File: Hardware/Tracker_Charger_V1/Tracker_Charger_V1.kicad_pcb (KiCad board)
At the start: 4 copper layers, 100 x 100 mm, 51 parts, among them J1 USB_C_USB20, J2 GSB3CN1130DSHR, J3 GSB3CN1130DSHR, J4 GSB3CN1130DSHR, J6 GSB3CN1130DSHR, J7 GSB3CN1130DSHR, SW1 SW_Push, SW2 SW_Push, SW3 SW_Push, SW4 SW_Push, SW5 SW_Push, SW6 SW_Push, U1 ESP32-C3-MINI-1-N4, U2 IN-PI15TAT5R5G5B, U3 RT8010, U6 IN-PI15TAT5R5G5B, U7 IN-PI15TAT5R5G5B, U8 IN-PI15TAT5R5G5B, U9 IN-PI15TAT5R5G5B

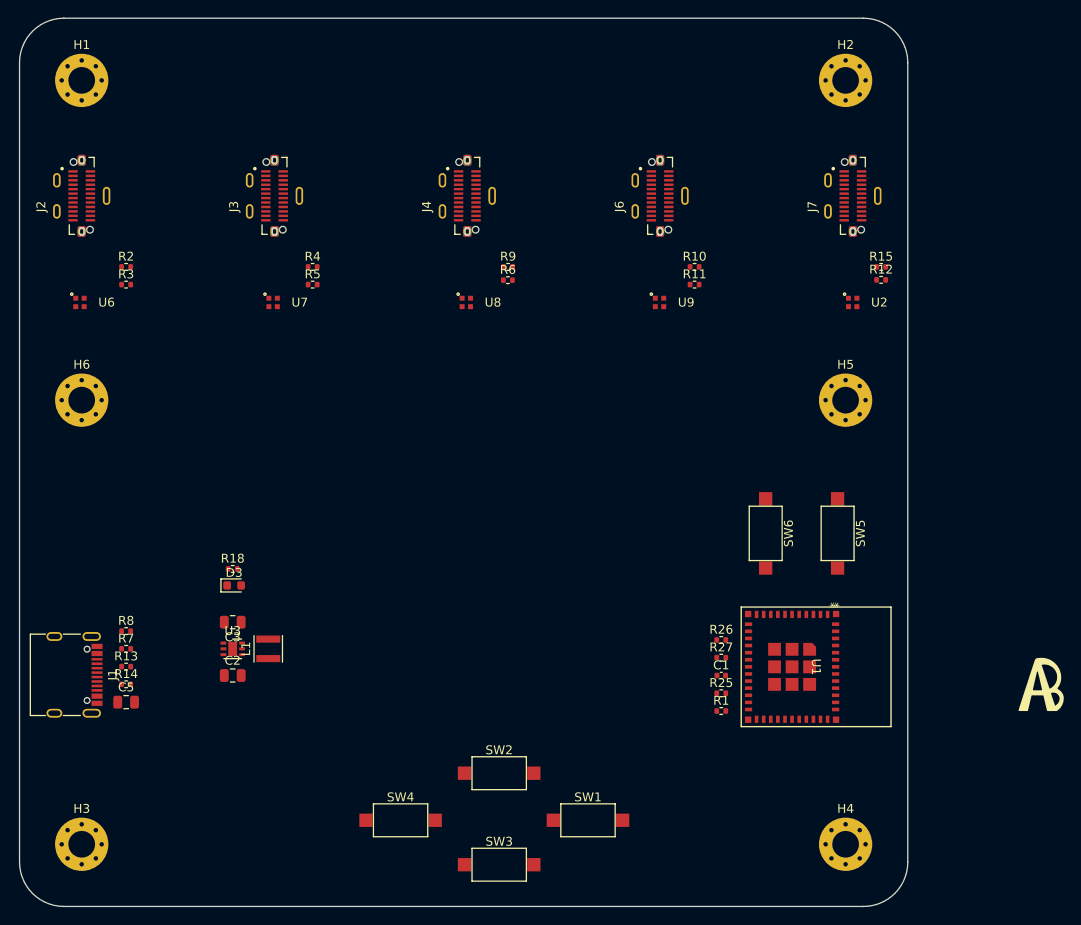
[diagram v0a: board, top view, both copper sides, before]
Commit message: Updated/Added Footprints
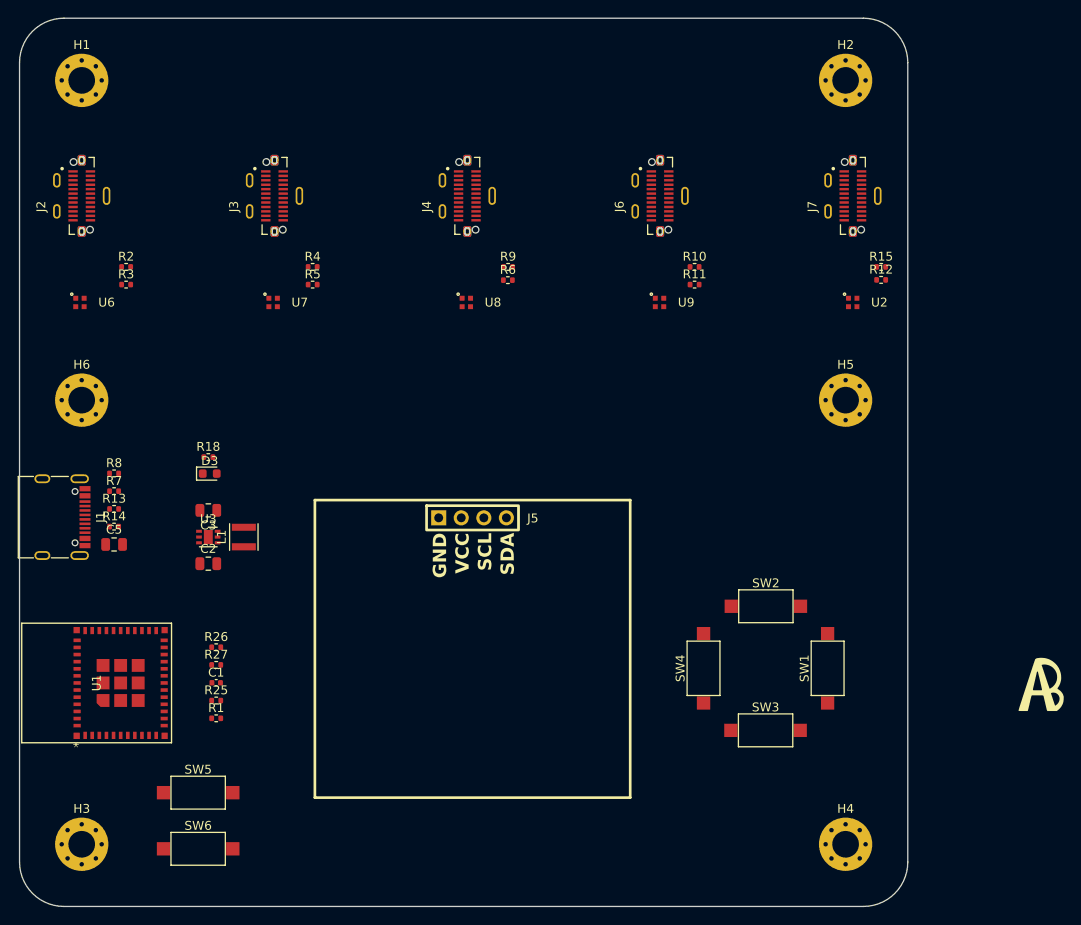
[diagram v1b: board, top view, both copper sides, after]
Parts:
- added J5: SSD1306_I2C_128x64, 00_tracker_fp:SSD1306_12864_I2C_13in, F.Cu at (141.0, 106.2)
- moved U1 81.0 mm to (98.7, 124.8), turned to 90 degrees
- moved SW5 77.7 mm to (110.1, 137.2), turned to 0 degrees
- moved SW6 73.1 mm to (110.1, 143.5), turned to 0 degrees
- moved C1 56.9 mm to (112.1, 124.8)
- moved R1 56.9 mm to (112.1, 128.8)
- moved R25 56.9 mm to (112.1, 126.8)
- moved R26 56.9 mm to (112.1, 120.8)
- moved R27 56.9 mm to (112.1, 122.8)
- moved SW4 38.2 mm to (167.0, 123.2), turned to 90 degrees
- moved SW2 35.4 mm to (174.0, 116.2)
- moved SW3 33.6 mm to (174.0, 130.2)
- moved SW1 31.9 mm to (181.0, 123.2), turned to 90 degrees
- moved C5 17.8 mm to (100.6, 109.2)
- moved J1 17.8 mm to (93.6, 106.2)
- moved R13 17.8 mm to (100.6, 105.2)
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
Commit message: Charger PCB Update
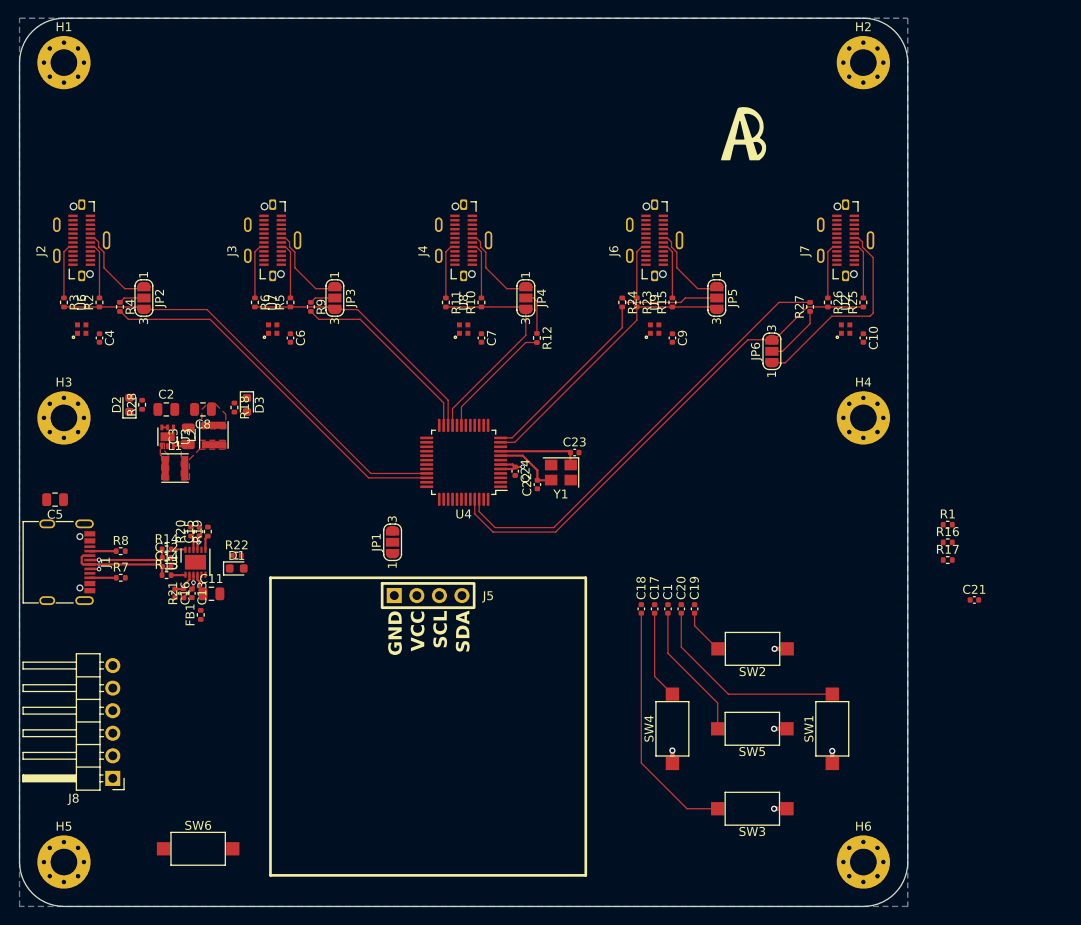
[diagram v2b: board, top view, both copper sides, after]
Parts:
- added C10: 0.1u, Capacitor_SMD:C_0402_1005Metric, F.Cu at (185.0, 86.0)
- added C11: 10u, Capacitor_SMD:C_0805_2012Metric, F.Cu at (111.6, 114.8)
- added C12: 47p, Capacitor_SMD:C_0402_1005Metric, F.Cu at (106.6, 110.8)
- added C13: 0.1u, Capacitor_SMD:C_0402_1005Metric, F.Cu at (109.4, 114.8)
- added C14: 47p, Capacitor_SMD:C_0402_1005Metric, F.Cu at (106.6, 111.8)
- added C15: 0.1u, Capacitor_SMD:C_0402_1005Metric, F.Cu at (110.3, 107.8)
- added C16: 0.1u, Capacitor_SMD:C_0402_1005Metric, F.Cu at (107.5, 114.8)
- added C17: 0.1u, Capacitor_SMD:C_0402_1005Metric, F.Cu at (161.5, 116.5)
- added C18: 0.1u, Capacitor_SMD:C_0402_1005Metric, F.Cu at (160.0, 116.5)
- added C19: 0.1u, Capacitor_SMD:C_0402_1005Metric, F.Cu at (166.0, 116.5)
- added C20: 0.1u, Capacitor_SMD:C_0402_1005Metric, F.Cu at (164.5, 116.5)
- added C21: 0.1u, Capacitor_SMD:C_0402_1005Metric, F.Cu at (197.5, 115.5)
- added C22: 27p, Capacitor_SMD:C_0402_1005Metric, F.Cu at (148.3, 102.5)
- added C23: 27p, Capacitor_SMD:C_0402_1005Metric, F.Cu at (152.5, 98.9)
- added C24: 1u, Capacitor_SMD:C_0402_1005Metric, F.Cu at (145.8, 101.0)
- added C4: 0.1u, Capacitor_SMD:C_0402_1005Metric, F.Cu at (99.0, 86.0)
- added C6: 0.1u, Capacitor_SMD:C_0402_1005Metric, F.Cu at (120.5, 86.0)
- added C7: 0.1u, Capacitor_SMD:C_0402_1005Metric, F.Cu at (142.0, 86.0)
- added C8: 10u, Capacitor_SMD:C_0805_2012Metric, F.Cu at (110.7, 94.0)
- added C9: 0.1u, Capacitor_SMD:C_0402_1005Metric, F.Cu at (163.5, 86.0)
- added D1: GREEN, LED_SMD:LED_0603_1608Metric, F.Cu at (114.5, 112.0)
- added D2: GREEN, LED_SMD:LED_0603_1608Metric, F.Cu at (102.4, 93.5)
- added FB1: 600@100MHz, Resistor_SMD:R_0402_1005Metric, F.Cu at (110.4, 117.2)
- added J8: ST-LINK, Connector_PinHeader_2.54mm:PinHeader_1x06_P2.54mm_Horizontal, F.Cu at (100.5, 135.6)
- added JP1: SolderJumper_3_Open, Jumper:SolderJumper-3_P1.3mm_Open_RoundedPad1.0x1.5mm_NumberLabels, F.Cu at (132.0, 109.0)
- added JP2: SolderJumper_3_Open, Jumper:SolderJumper-3_P1.3mm_Open_RoundedPad1.0x1.5mm_NumberLabels, F.Cu at (104.0, 81.5)
- added JP3: SolderJumper_3_Open, Jumper:SolderJumper-3_P1.3mm_Open_RoundedPad1.0x1.5mm_NumberLabels, F.Cu at (125.5, 81.5)
- added JP4: SolderJumper_3_Open, Jumper:SolderJumper-3_P1.3mm_Open_RoundedPad1.0x1.5mm_NumberLabels, F.Cu at (147.0, 81.5)
- added JP5: SolderJumper_3_Open, Jumper:SolderJumper-3_P1.3mm_Open_RoundedPad1.0x1.5mm_NumberLabels, F.Cu at (168.5, 81.5)
- added JP6: SolderJumper_3_Open, Jumper:SolderJumper-3_P1.3mm_Open_RoundedPad1.0x1.5mm_NumberLabels, F.Cu at (174.7, 87.5)
- added L2: 4.7uH, Inductor_SMD:L_Taiyo-Yuden_NR-30xx, F.Cu at (111.9, 96.9)
- added R16: 4.7k, Resistor_SMD:R_0402_1005Metric, F.Cu at (194.5, 109.0)
- added R17: 4.7k, Resistor_SMD:R_0402_1005Metric, F.Cu at (194.5, 111.0)
- added R19: 330, Resistor_SMD:R_0402_1005Metric, F.Cu at (111.2, 107.8)
- added R20: 330, Resistor_SMD:R_0402_1005Metric, F.Cu at (109.3, 107.8)
- added R21: 1k, Resistor_SMD:R_0402_1005Metric, F.Cu at (108.5, 114.8)
- added R22: 1k, Resistor_SMD:R_0402_1005Metric, F.Cu at (114.5, 110.5)
- added R23: 330, Resistor_SMD:R_0402_1005Metric, F.Cu at (159.5, 82.0)
- added R24: 330, Resistor_SMD:R_0402_1005Metric, F.Cu at (157.8, 82.0)
- added R28: 1k, Resistor_SMD:R_0402_1005Metric, F.Cu at (103.8, 93.5)
- added U4: STM32G070CBTx, Package_QFP:LQFP-48_7x7mm_P0.5mm, F.Cu at (140.0, 100.0)
- added Y1: 8MHz, Crystal:Crystal_SMD_Abracon_ABM8G-4Pin_3.2x2.5mm, F.Cu at (150.9, 101.2)
- C1: value 1u -> 0.1u
- J2, J3, J4, J6, J7: footprint 00_tracker_fp:AMPHENOL_GSB3CN1130DSHR -> 00_tracker_fp:AMPHENOL_GSB3CN1130DSHR_NEW1
- R10, R11, R12, R15, R2, R3, R4, R5, R6, R9: value 1k -> 330
- R18: value 2.2k -> 1k
- R25, R26, R27: value 10k -> 330
- U1: value ESP32-C3-MINI-1-N4 -> FT234XD-T; footprint 00_tracker_fp:ESP32-C3-MINI-1_EXP -> Package_DFN_QFN:DFN-12-1EP_3x3mm_P0.45mm_EP1.66x2.38mm
- moved H5 102.2 mm to (95.0, 145.0)
- moved H6 102.2 mm to (185.0, 145.0)
- moved R25 85.5 mm to (185.0, 82.0), turned to 90 degrees
- moved R1 85.2 mm to (194.5, 107.0)
- moved R26 79.0 mm to (181.0, 82.0), turned to -90 degrees
- moved R27 78.1 mm to (179.0, 82.5), turned to 90 degrees
- moved LG1 70.5 mm to (171.5, 63.0)
- moved SW5 62.8 mm to (172.5, 130.0), turned to 180 degrees
- moved C1 51.5 mm to (163.0, 116.5), turned to 90 degrees
- moved H3 48.0 mm to (95.0, 95.0)
- moved H4 48.0 mm to (185.0, 95.0)
- moved R12 39.3 mm to (148.2, 86.0), turned to -90 degrees
- moved R6 28.6 mm to (116.5, 82.0), turned to -90 degrees
- moved R11 28.1 mm to (138.0, 82.0), turned to -90 degrees
- moved R10 24.3 mm to (142.0, 82.0), turned to 90 degrees
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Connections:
- C1 pad 1: /RST_N -> /SW5
- C3 pad 1: +3.3V -> /3V3_RAW
- H1 pad 1: (no net) -> unconnected-(H1-Pad1)
- H2 pad 1: (no net) -> unconnected-(H2-Pad1)
- H3 pad 1: (no net) -> unconnected-(H3-Pad1)
- H4 pad 1: (no net) -> unconnected-(H4-Pad1)
- H5 pad 1: (no net) -> unconnected-(H5-Pad1)
- H6 pad 1: (no net) -> unconnected-(H6-Pad1)
- J1 pad A6: Net-(J1-D+-PadA6) -> /USB_D+
- J1 pad A7: Net-(J1-D--PadA7) -> /USB_D-
- J1 pad B6: Net-(J1-D+-PadA6) -> /USB_D+
- J1 pad B7: Net-(J1-D--PadA7) -> /USB_D-
- J2 pad B6: unconnected-(J2-DP2-PadB6) -> Net-(J2-DP2)
- J3 pad B6: unconnected-(J3-DP2-PadB6) -> Net-(J3-DP2)
- J4 pad B6: unconnected-(J4-DP2-PadB6) -> Net-(J4-DP2)
- J5 pad 2: VBUS -> Net-(J5-VCC)
- J6 pad B6: unconnected-(J6-DP2-PadB6) -> Net-(J6-DP2)
- J7 pad B6: unconnected-(J7-DP2-PadB6) -> Net-(J7-DP2)
- L1 pad 2: +3.3V -> /3V3_RAW
- R1 pad 2: /RST_N -> /MCU_NRST
- R10 pad 1: Net-(J6-SBU2) -> /BAND_TX3
- R10 pad 2: /SBU_P4 -> Net-(J4-SBU2)
- R11 pad 1: Net-(J6-SBU1) -> Net-(J4-SBU1)
- R11 pad 2: /SBU_P4 -> /BAND_TX3
- R12 pad 1: Net-(J7-SBU2) -> Net-(JP4-C)
- R12 pad 2: /SBU_P5 -> /BAND_RX3
- R13 pad 1: Net-(J1-D--PadA7) -> /USB_D-
- R13 pad 2: /USB_D- -> Net-(U1-USBDM)
- R14 pad 1: Net-(J1-D+-PadA6) -> /USB_D+
- R14 pad 2: /USB_D+ -> Net-(U1-USBDP)
- R15 pad 1: Net-(J7-SBU1) -> /BAND_TX4
- R15 pad 2: /SBU_P5 -> Net-(J6-SBU2)
- R2 pad 1: Net-(J2-SBU2) -> /BAND_TX1
- R2 pad 2: /SBU_P1 -> Net-(J2-SBU2)
- R25 pad 1: +3.3V -> /BAND_TX5
- R25 pad 2: /BOOT_N -> Net-(J7-SBU2)
- R26 pad 1: +3.3V -> Net-(J7-SBU1)
- R26 pad 2: Net-(U1-GPIO8) -> /BAND_TX5
- R27 pad 1: +3.3V -> Net-(JP6-C)
- R27 pad 2: Net-(U1-GPIO2,_ADC1_CH2,_FSPIQ) -> /BAND_RX5
- R3 pad 2: /SBU_P1 -> /BAND_TX1
- R4 pad 1: Net-(J3-SBU2) -> Net-(JP2-C)
- R4 pad 2: /SBU_P2 -> /BAND_RX1
- R5 pad 1: Net-(J3-SBU1) -> /BAND_TX2
- R5 pad 2: /SBU_P2 -> Net-(J3-SBU2)
- R6 pad 1: Net-(J4-SBU2) -> Net-(J3-SBU1)
- R6 pad 2: /SBU_P3 -> /BAND_TX2
- R9 pad 1: Net-(J4-SBU1) -> Net-(JP3-C)
- R9 pad 2: /SBU_P3 -> /BAND_RX2
- SW5 pad 2: /RST_N -> /SW5
- SW6 pad 1: GND -> /MCU_NRST
- SW6 pad 2: /BOOT_N -> GND
- U1 pad 1: GND -> Net-(U1-USBDM)
- U1 pad 10: unconnected-(U1-NC-Pad10) -> Net-(U1-RXD)
- U1 pad 11: GND -> unconnected-(U1-CTS#-Pad11)
- U1 pad 12: unconnected-(U1-GPIO0,_ADC1_CH0,_XTAL_32K_P-Pad12) -> Net-(U1-USBDP)
- U1 pad 13: unconnected-(U1-GPIO1,_ADC1_CH1,_XTAL_32K_N-Pad13) -> GND
- U1 pad 2: GND -> Net-(U1-~{RESET}#)
- U1 pad 3: +3.3V -> Net-(U1-3V3OUT)
- U1 pad 4: unconnected-(U1-NC-Pad4) -> Net-(U1-VCC)
- U1 pad 5: Net-(U1-GPIO2,_ADC1_CH2,_FSPIQ) -> GND
- U1 pad 6: unconnected-(U1-GPIO3,_ADC1_CH3-Pad6) -> Net-(D1-K)
- U1 pad 7: unconnected-(U1-NC-Pad7) -> Net-(U1-TXD)
- U1 pad 8: /RST_N -> unconnected-(U1-RTS#-Pad8)
- U1 pad 9: unconnected-(U1-NC-Pad9) -> Net-(U1-3V3OUT)
- U3 pad 6: +3.3V -> /3V3_RAW
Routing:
- net /BAND_TX5: track 0.00 -> 56.7 mm
- net /BAND_RX5: track 0.00 -> 49.9 mm
- net /BAND_TX1: track 0.00 -> 49.0 mm
- net /BAND_RX1: track 0.00 -> 42.3 mm
- net /BAND_TX4: track 0.00 -> 32.0 mm
- net /BAND_TX2: track 0.00 -> 29.3 mm
- net /SW3: track 0.00 -> 27.6 mm
- net /BAND_TX3: track 0.00 -> 26.0 mm
- net Net-(J7-DP2): track 0.00 -> 23.3 mm
- net /SW1: track 0.00 -> 23.0 mm
- net /BAND_RX2: track 0.00 -> 21.7 mm
- net /BAND_RX4: track 0.00 -> 21.2 mm
- net /SW5: track 0.00 -> 15.3 mm
- net /BAND_RX3: track 0.00 -> 13.6 mm
- net /USB_D-: track 0.00 -> 11.9 mm
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- added copper zone on F.Cu, net +3.3V
- added copper zone on F.Cu, net /3V3_RAW
- added copper zone on F.Cu, net /LX
- added copper zone on B.Cu, net GND
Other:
- copper layers 4 -> 2

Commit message: SCH & PCB Updated
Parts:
- added C25: 0.1u, Capacitor_SMD:C_0402_1005Metric, F.Cu at (103.4, 70.8)
- added C26: 0.1u, Capacitor_SMD:C_0402_1005Metric, F.Cu at (103.0, 73.5)
- added C27: 0.1u, Capacitor_SMD:C_0402_1005Metric, F.Cu at (101.5, 70.8)
- added C28: 0.1u, Capacitor_SMD:C_0402_1005Metric, F.Cu at (107.5, 74.2)
- added C29: 0.1u, Capacitor_SMD:C_0402_1005Metric, F.Cu at (135.6, 95.0)
- added C30: 0.1u, Capacitor_SMD:C_0402_1005Metric, F.Cu at (124.9, 70.8)
- added C31: 0.1u, Capacitor_SMD:C_0402_1005Metric, F.Cu at (124.5, 73.5)
- added C32: 0.1u, Capacitor_SMD:C_0402_1005Metric, F.Cu at (123.0, 70.8)
- added C33: 0.1u, Capacitor_SMD:C_0402_1005Metric, F.Cu at (129.0, 74.1)
- added C34: 0.1u, Capacitor_SMD:C_0402_1005Metric, F.Cu at (139.4, 93.5)
- added C35: 0.1u, Capacitor_SMD:C_0402_1005Metric, F.Cu at (146.4, 70.8)
- added C36: 0.1u, Capacitor_SMD:C_0402_1005Metric, F.Cu at (145.9, 73.5)
- added C37: 0.1u, Capacitor_SMD:C_0402_1005Metric, F.Cu at (144.6, 70.8)
- added C38: 0.1u, Capacitor_SMD:C_0402_1005Metric, F.Cu at (150.5, 74.1)
- added C39: 0.1u, Capacitor_SMD:C_0402_1005Metric, F.Cu at (140.5, 93.5)
- added C40: 0.1u, Capacitor_SMD:C_0402_1005Metric, F.Cu at (167.9, 70.8)
- added C41: 0.1u, Capacitor_SMD:C_0402_1005Metric, F.Cu at (167.4, 73.5)
- added C42: 0.1u, Capacitor_SMD:C_0402_1005Metric, F.Cu at (166.1, 70.8)
- added C43: 0.1u, Capacitor_SMD:C_0402_1005Metric, F.Cu at (171.9, 74.2)
- added C44: 0.1u, Capacitor_SMD:C_0402_1005Metric, F.Cu at (141.6, 93.5)
- added C45: 0.1u, Capacitor_SMD:C_0402_1005Metric, F.Cu at (178.6, 63.6)
- added C46: 0.1u, Capacitor_SMD:C_0402_1005Metric, F.Cu at (179.0, 60.9)
- added C47: 0.1u, Capacitor_SMD:C_0402_1005Metric, F.Cu at (180.4, 63.6)
- added C48: 0.1u, Capacitor_SMD:C_0402_1005Metric, F.Cu at (174.5, 60.2)
- added C49: 0.1u, Capacitor_SMD:C_0402_1005Metric, F.Cu at (142.6, 93.5)
- added C50: 1u, Capacitor_SMD:C_0402_1005Metric, F.Cu at (146.4, 101.0)
- added FB2: 600@100MHz, Resistor_SMD:R_0402_1005Metric, F.Cu at (147.4, 101.9)
- added R29: 33m, Resistor_SMD:R_1206_3216Metric, F.Cu at (102.5, 68.9)
- added R30: 10k, Resistor_SMD:R_0402_1005Metric, F.Cu at (107.6, 70.8)
- added R31: 33m, Resistor_SMD:R_1206_3216Metric, F.Cu at (124.0, 68.9)
- added R32: 10k, Resistor_SMD:R_0402_1005Metric, F.Cu at (129.1, 70.8)
- added R33: 33m, Resistor_SMD:R_1206_3216Metric, F.Cu at (145.4, 68.9)
- added R34: 10k, Resistor_SMD:R_0402_1005Metric, F.Cu at (150.6, 70.8)
- added R35: 33m, Resistor_SMD:R_1206_3216Metric, F.Cu at (166.9, 68.9)
- added R36: 10k, Resistor_SMD:R_0402_1005Metric, F.Cu at (172.1, 70.8)
- added R37: 33m, Resistor_SMD:R_1206_3216Metric, F.Cu at (179.5, 65.5)
- added R38: 10k, Resistor_SMD:R_0402_1005Metric, F.Cu at (174.3, 63.6)
- added R39: 100k, Resistor_SMD:R_0402_1005Metric, F.Cu at (101.0, 73.0)
- added R40: 100k, Resistor_SMD:R_0402_1005Metric, F.Cu at (113.8, 74.4)
- added R41: 100k, Resistor_SMD:R_0402_1005Metric, F.Cu at (135.3, 74.4)
- added R42: 100k, Resistor_SMD:R_0402_1005Metric, F.Cu at (156.8, 74.4)
- added R43: 100k, Resistor_SMD:R_0402_1005Metric, F.Cu at (178.3, 74.4)
- added U10: INA180A3, Package_TO_SOT_SMD:SOT-23-5, F.Cu at (126.7, 73.5)
- added U11: INA180A3, Package_TO_SOT_SMD:SOT-23-5, F.Cu at (148.2, 73.5)
- added U12: INA180A3, Package_TO_SOT_SMD:SOT-23-5, F.Cu at (169.7, 73.5)
- added U13: INA180A3, Package_TO_SOT_SMD:SOT-23-5, F.Cu at (176.8, 60.9)
- added U5: INA180A3, Package_TO_SOT_SMD:SOT-23-5, F.Cu at (105.2, 73.5)
- J8: footprint Connector_PinHeader_2.54mm:PinHeader_1x06_P2.54mm_Horizontal -> Connector_PinHeader_2.54mm:PinHeader_1x08_P2.54mm_Horizontal
- moved R1 61.0 mm to (133.5, 107.0), turned to 180 degrees
- moved C21 54.0 mm to (146.4, 98.1)
- moved R17 48.8 mm to (146.2, 104.2), turned to 180 degrees
- moved R16 48.5 mm to (146.2, 105.5), turned to 180 degrees
- moved SW1 12.7 mm to (172.5, 121.0), turned to 180 degrees
- moved SW2 12.7 mm to (181.5, 130.0), turned to 90 degrees
- moved SW6 8.41 mm to (111.0, 135.2), turned to -90 degrees
- moved R28 8.25 mm to (104.3, 101.8)
- moved D2 5.50 mm to (104.3, 98.7), turned to -90 degrees
- moved C22 4.46 mm to (152.2, 100.3), turned to 180 degrees
- moved D3 4.28 mm to (117.5, 97.3), turned to 90 degrees
- moved C23 4.02 mm to (148.6, 97.9), turned to -90 degrees
- moved R27 3.75 mm to (177.7, 86.0)
- moved Y1 3.49 mm to (150.8, 97.7), turned to -90 degrees
- moved R18 3.39 mm to (117.5, 94.3)
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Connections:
- J2 pad A4: VBUS -> /VBUS1
- J2 pad A9: VBUS -> /VBUS1
- J2 pad B4: VBUS -> /VBUS1
- J2 pad B5: unconnected-(J2-CC2-PadB5) -> /PRES1
- J2 pad B9: VBUS -> /VBUS1
- J3 pad A4: VBUS -> /VBUS2
- J3 pad A5: unconnected-(J3-CC1-PadA5) -> /PRES2
- J3 pad A9: VBUS -> /VBUS2
- J3 pad B4: VBUS -> /VBUS2
- J3 pad B9: VBUS -> /VBUS2
- J4 pad A4: VBUS -> /VBUS3
- J4 pad A5: unconnected-(J4-CC1-PadA5) -> /PRES3
- J4 pad A9: VBUS -> /VBUS3
- J4 pad B4: VBUS -> /VBUS3
- J4 pad B9: VBUS -> /VBUS3
- J6 pad A4: VBUS -> /VBUS4
- J6 pad A5: unconnected-(J6-CC1-PadA5) -> /PRES4
- J6 pad A9: VBUS -> /VBUS4
- J6 pad B4: VBUS -> /VBUS4
- J6 pad B9: VBUS -> /VBUS4
- J7 pad A4: VBUS -> /VBUS5
- J7 pad A5: unconnected-(J7-CC1-PadA5) -> /PRES5
- J7 pad A9: VBUS -> /VBUS5
- J7 pad B4: VBUS -> /VBUS5
- J7 pad B9: VBUS -> /VBUS5
- J8 pad 6: unconnected-(J8-Pin_6-Pad6) -> GND
- JP1 pad 1: +3.3V -> VBUS
- JP1 pad 3: VBUS -> +3.3V
- U4 pad 1: unconnected-(U4-PC13-Pad1) -> /PRES5
- U4 pad 15: unconnected-(U4-PA4-Pad15) -> /I_SENS5
- U4 pad 16: unconnected-(U4-PA5-Pad16) -> /I_SENS4
- U4 pad 17: unconnected-(U4-PA6-Pad17) -> /I_SENS3
- U4 pad 18: unconnected-(U4-PA7-Pad18) -> /I_SENS2
- U4 pad 24: unconnected-(U4-PB12-Pad24) -> /I_SENS1
- U4 pad 25: unconnected-(U4-PB13-Pad25) -> /PRES3
- U4 pad 26: unconnected-(U4-PB14-Pad26) -> /PRES2
- U4 pad 27: unconnected-(U4-PB15-Pad27) -> /PRES4
- U4 pad 28: unconnected-(U4-PA8-Pad28) -> /PRES1
- U4 pad 39: unconnected-(U4-PD1-Pad39) -> /SW3
- U4 pad 40: unconnected-(U4-PD2-Pad40) -> /SW4
- U4 pad 41: unconnected-(U4-PD3-Pad41) -> /SW5
- U4 pad 42: unconnected-(U4-PB3-Pad42) -> /SW2
- U4 pad 43: unconnected-(U4-PB4-Pad43) -> /SW1
- U4 pad 44: unconnected-(U4-PB5-Pad44) -> /RGB_LED
- U4 pad 47: unconnected-(U4-PB8-Pad47) -> /MCU_SCL
- U4 pad 48: unconnected-(U4-PB9-Pad48) -> /MCU_SDA
- U4 pad 5: +3.3V -> Net-(U4-VREF+)
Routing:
- net VBUS: track 0.65 -> 108.5 mm
- net /I_SENS5: track 0.00 -> 95.7 mm, vias 0 -> 4
- net /MCU_SDA: track 0.00 -> 65.9 mm, vias 0 -> 1
- net /MCU_SCL: track 0.00 -> 63.1 mm, vias 0 -> 1
- net /MCU_NRST: track 0.00 -> 61.0 mm, vias 0 -> 2
- net /RGB_LED: track 0.00 -> 53.0 mm, vias 0 -> 2
- net /PRES5: track 0.00 -> 51.7 mm
- net /I_SENS4: track 0.00 -> 50.8 mm, vias 0 -> 2
- net /PRES1: track 0.00 -> 50.1 mm
- net /SW2: track 5.12 -> 55.2 mm
- net /ST_SWDIO: track 0.00 -> 48.0 mm, vias 0 -> 2
- net /I_SENS1: track 0.00 -> 46.9 mm, vias 0 -> 2
- net /ST_SWCLK: track 0.00 -> 45.0 mm, vias 0 -> 2
- net /PRES4: track 0.00 -> 40.2 mm
- net /PRES2: track 0.00 -> 40.2 mm
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- added copper zone on F.Cu, net /VBUS1
- added copper zone on F.Cu, net /VBUS2
- added copper zone on F.Cu, net /VBUS3
- added copper zone on F.Cu, net /VBUS4
- added copper zone on F.Cu, net /VBUS5
- added copper zone on F.Cu, net GND
- added copper zone on F.Cu, net VBUS
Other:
- board text added: "3V3"
- board text added: "CLK"
- board text added: "DIO"
- board text added: "GND"
- board text added: "MCU RESET"
- board text added: "RST"
- board text added: "SCL"
- board text added: "SDA"

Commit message: PCB Layout Finalized
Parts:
- added LG2: ~, 00_tracker_fp:run_silk_14mm, F.Cu at (110.8, 59.1)
- added LG3: ~, 00_tracker_fp:bench_silk_14mm, F.Cu at (174.7, 103.2)
- added LG5: ~, 00_tracker_fp:hike_silk_14mm, F.Cu at (160.1, 59.1)
- added LG6: ~, 00_tracker_fp:squat_silk_14mm, F.Cu at (135.0, 59.1)
- moved LG1 81.3 mm to (160.2, 143.6)
- moved R18 7.45 mm to (117.3, 101.8)
- moved SW6 6.99 mm to (110.2, 142.1), turned to 0 degrees
- moved R16 4.22 mm to (149.8, 103.3), turned to -90 degrees
- moved R1 2.66 mm to (135.3, 105.0), turned to 90 degrees
- moved R17 2.49 mm to (148.5, 103.3), turned to -90 degrees
- moved D3 1.32 mm to (117.3, 98.7)
- moved FB2 1.22 mm to (146.7, 100.9)
- moved C50 0.90 mm to (146.5, 101.8)
- moved C24 0.15 mm to (146.7, 100.0)
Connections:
- C17 pad 1: /SW4 -> /SW3
- C18 pad 1: /SW3 -> /SW4
- D3 pad 1: GND -> Net-(D3-K)
- D3 pad 2: Net-(D3-A) -> +3.3V
- J8 pad 1: +3.3V -> /ST_SWCLK
- J8 pad 2: /ST_SWCLK -> GND
- J8 pad 3: GND -> /ST_SWDIO
- J8 pad 4: /ST_SWDIO -> /MCU_NRST
- J8 pad 5: /MCU_NRST -> GND
- J8 pad 6: GND -> /MCU_SCL
- J8 pad 7: /MCU_SCL -> /MCU_SDA
- J8 pad 8: /MCU_SDA -> +3.3V
- R18 pad 1: +3.3V -> Net-(D3-K)
- R18 pad 2: Net-(D3-A) -> GND
- U4 pad 1: /PRES5 -> unconnected-(U4-PC13-Pad1)
- U4 pad 38: unconnected-(U4-PD0-Pad38) -> /PRES5
- U4 pad 39: /SW3 -> /SW4
- U4 pad 40: /SW4 -> /SW3
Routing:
- net +3.3V: track 27.8 -> 233.8 mm, vias 12 -> 15
- net /MCU_NRST: track 61.0 -> 82.1 mm
- net GND: track 40.1 -> 54.1 mm, vias 30 -> 69
- net /PRES5: track 51.7 -> 60.5 mm
- net /MCU_SCL: track 63.1 -> 66.9 mm
- net /SW3: track 58.5 -> 55.3 mm
- net /MCU_SDA: track 65.9 -> 68.3 mm
- net Net-(D3-K): track 0.00 -> 1.80 mm
- net Net-(D3-A): track 1.75 -> 0.00 mm
- net /RGB_LED2: track 20.9 -> 22.4 mm
- net /BAND_TX3: track 26.0 -> 27.4 mm
- net /SW4: track 41.3 -> 40.0 mm
- net /BAND_RX3: track 18.3 -> 17.1 mm
- net /ST_SWCLK: track 45.0 -> 43.9 mm
- net /ST_SWDIO: track 48.0 -> 46.9 mm
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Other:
- board text added: "1-Wire 2-Wire"
- board text added: "2-Wire 1-Wire"
- board text added: "2024"
- board text added: "3.3V"
- board text added: "5V"
- board text added: "JLCJLCJLCJLC"
- board text added: "SilhouetteSync Charger V1"
- board text added: "VBUS"
- board text added: "VCP ACT"
